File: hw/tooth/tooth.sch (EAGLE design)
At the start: 24 parts, among them X1 416F32022CKR

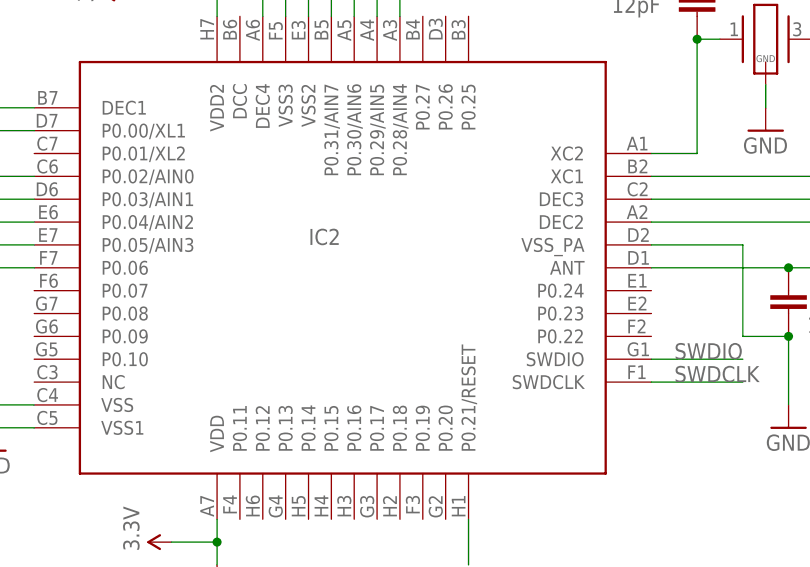
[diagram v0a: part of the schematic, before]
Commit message: hw: Add serial number of chip used on prototypes
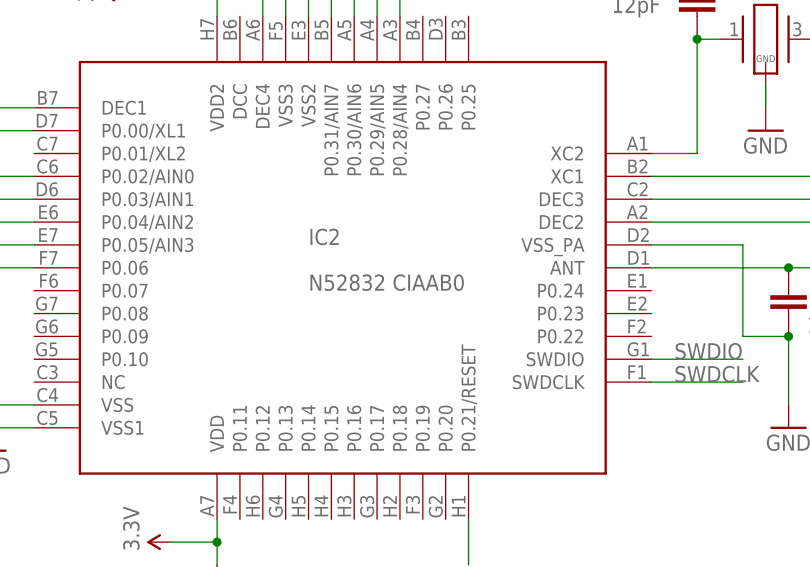
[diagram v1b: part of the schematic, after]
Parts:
- IC2: value (none) -> N52832 CIAAB0
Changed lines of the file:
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@@
 <part name="U$2" library="smartwatch" deviceset="SI1013" device=""/>
 <part name="P+2" library="SparkFun" deviceset="3.3V" device=""/>
-<part name="IC2" library="dan" deviceset="NRF52832" device=""/>
+<part name="IC2" library="dan" deviceset="NRF52832" device="" value="N52832 CIAAB0"/>
 <part name="C1" library="rcl" deviceset="C-EU" device="C0201" value="12pF"/>
 <part name="C2" library="rcl" deviceset="C-EU" device="C0201" value="12pF"/>

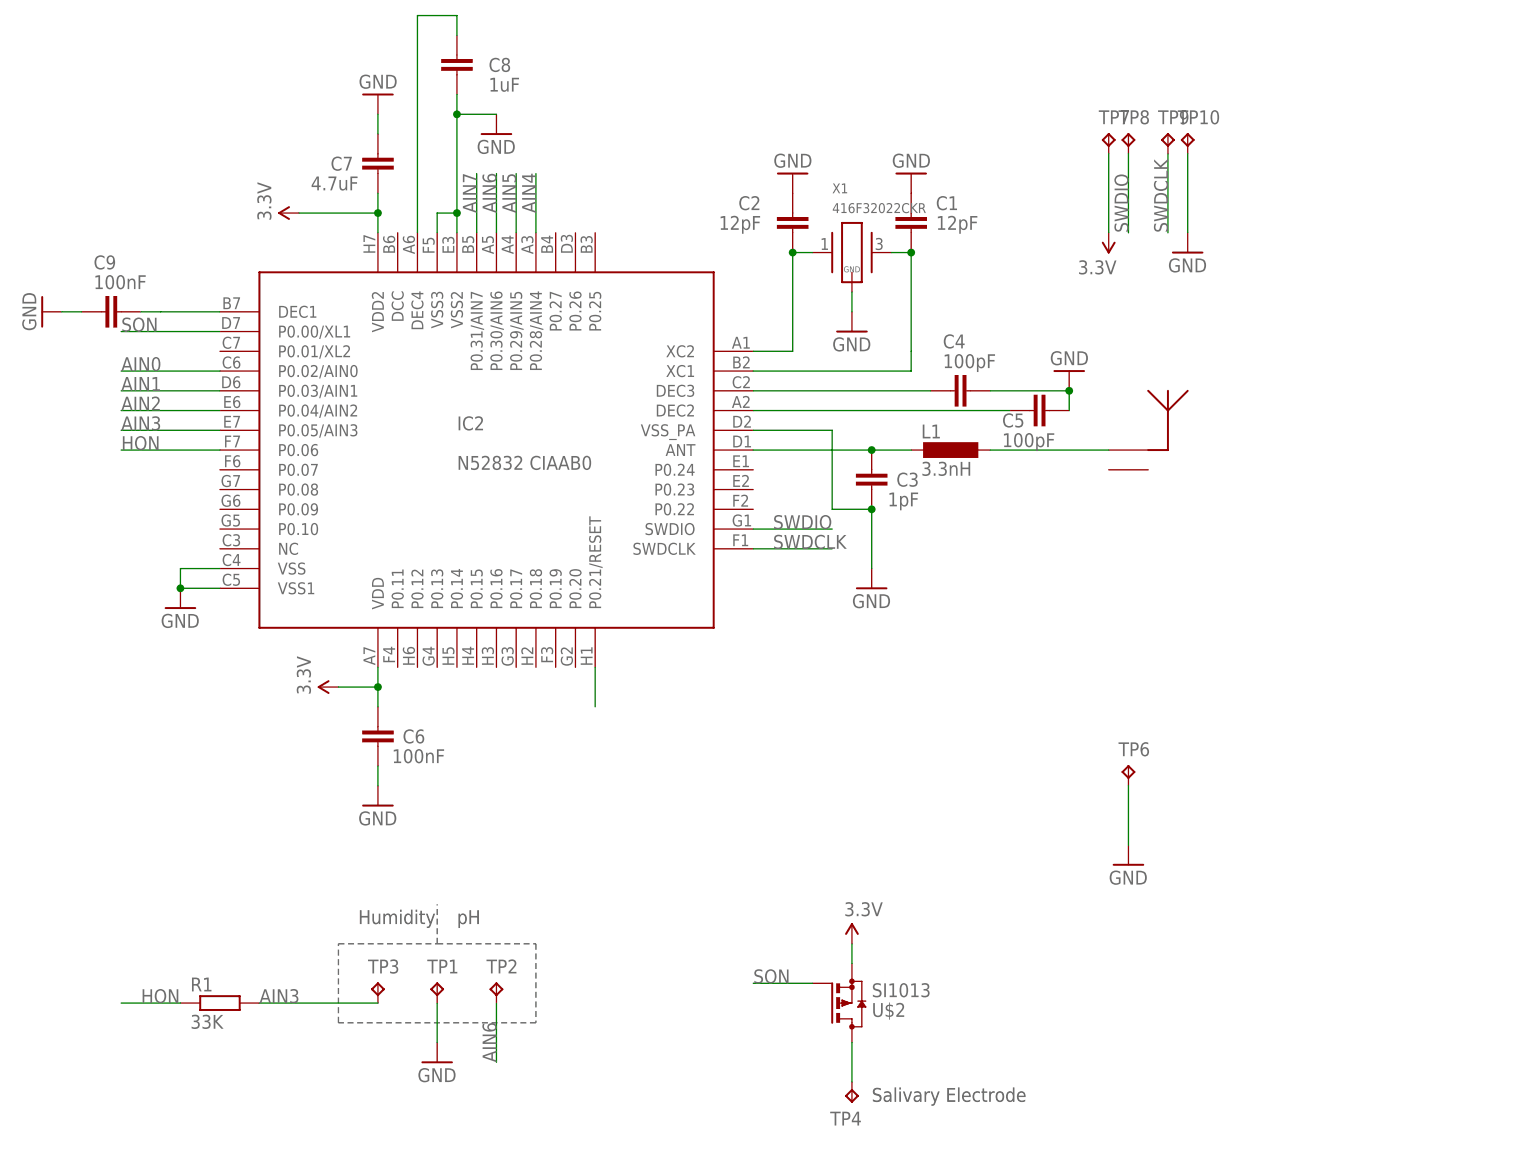
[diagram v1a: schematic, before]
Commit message: hw: Add new, smaller board revision
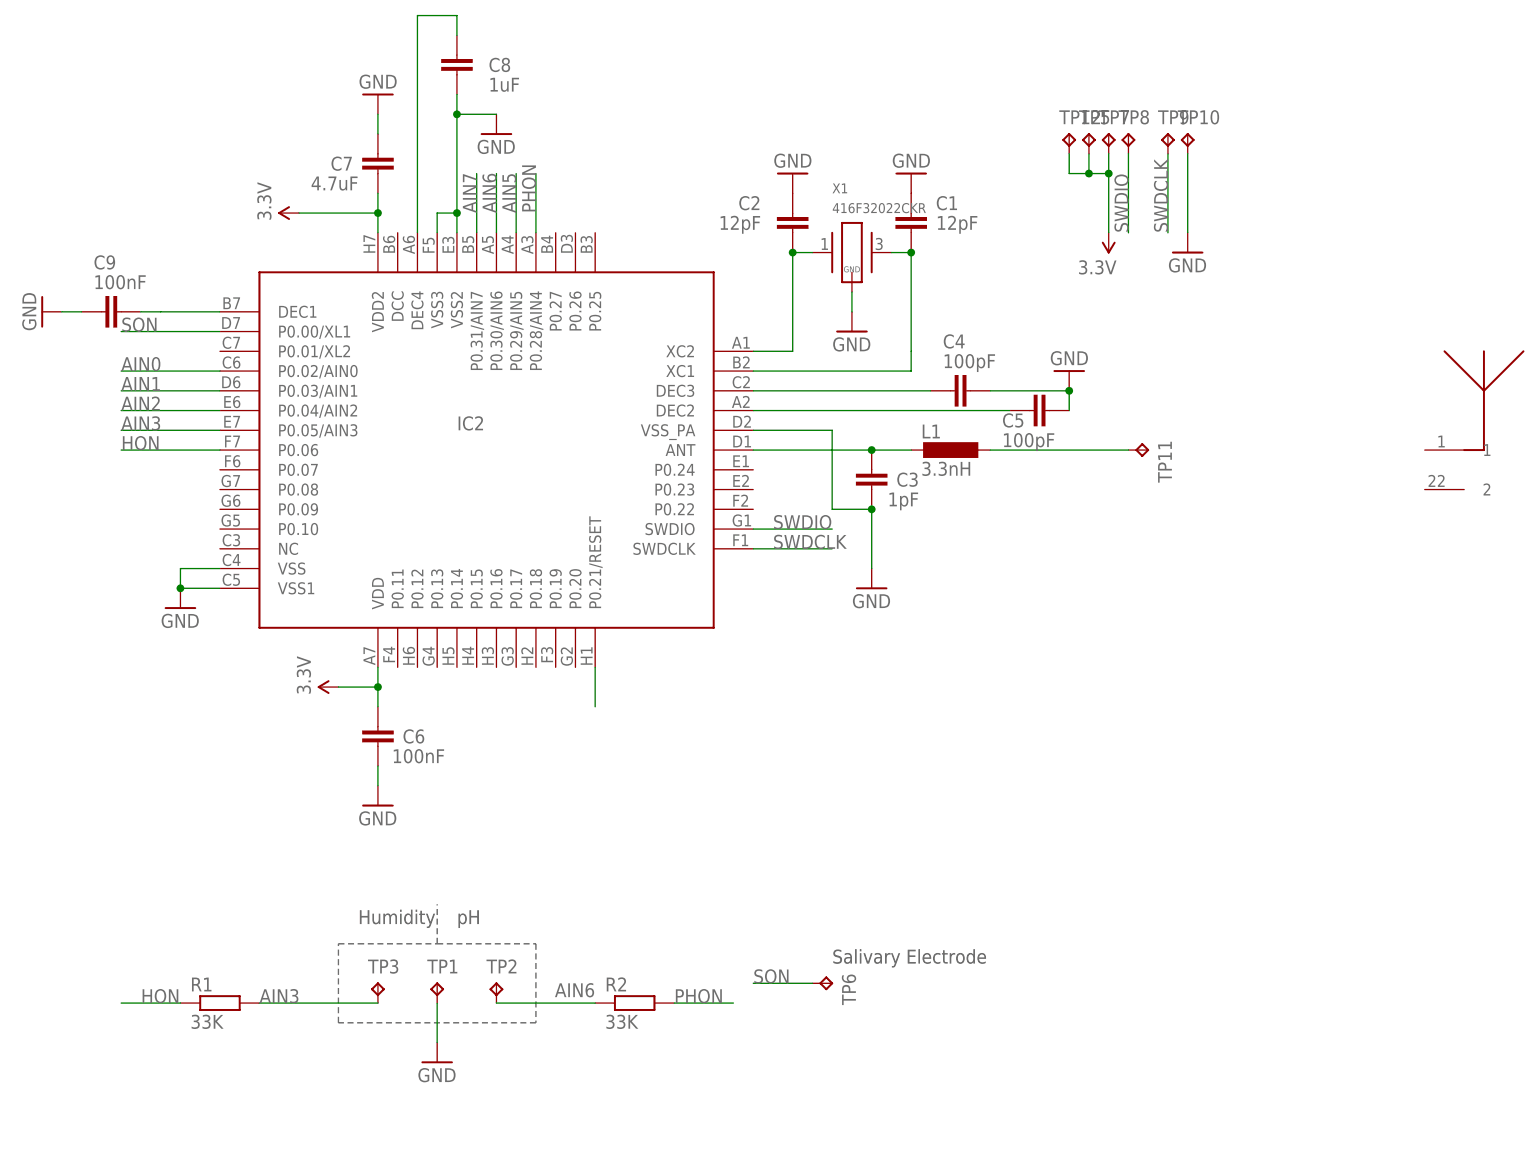
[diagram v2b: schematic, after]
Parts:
- removed TP4: TPTP10R, testpad:TPTP10R
- removed U$2: SI1013, smartwatch:SI1013
- removed U$3: 2450AT18A100, dan:2450AT18A100
- added R2: 33K, rcl:R-EU_R0201
- added TP11: TPTP10R, testpad:TPTP10R
- added TP12, TP5: TPTP15R, testpad:TPTP15R
- added U$1: ACA-102-T, dan:ACA-102-T
- IC2: value N52832 CIAAB0 -> (none)
- TP6: value TPTP20R -> TPTP15R; device testpad:TPTP20R -> testpad:TPTP15R
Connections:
- removed net AIN4: IC2.P0.28/AIN4
- removed net N$13: L1.1, U$3.P$1
- removed net N$5: TP4.TP, U$2.D
- new net N$3: L1.1, TP11.TP
- new net PHON: IC2.P0.28/AIN4, R2.2
- net 3.3V: now also TP12.TP, TP5.TP; no longer U$2.S
- net AIN6: now also R2.1
- net GND: no longer TP6.TP
- net SON: now also TP6.TP; no longer U$2.G
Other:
- moved on the sheet: TP6
